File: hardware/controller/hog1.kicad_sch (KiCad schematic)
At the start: 59 parts, among them J4 Conn_01x01, J5 Conn_01x01, J6 Conn_01x01, J7 Conn_01x03, J8 Conn_01x03, Q2 YJD60N04A, Q3 YJD60N04A, Q4 YJD60N04A, Q5 YJD60N04A, Q6 YJD60N04A, Q7 YJD60N04A, U10 LMV331, U11 LM2105D, U12 LMV331, U13 LM2105D, U14 LMV331, U9 LM2105D

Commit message: footprints, layout
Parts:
- removed J7, J8: Conn_01x03, symbol Connector_Generic:Conn_01x03
- removed Q2, Q3, Q4, Q5, Q6, Q7: YJD60N04A, symbol Simulation_SPICE:NMOS
- added J8: Conn_02x03_Odd_Even, Connector_PinHeader_2.54mm:PinHeader_2x03_P2.54mm_Horizontal, symbol Connector_Generic:Conn_02x03_Odd_Even
- added Q2, Q3, Q4, Q5, Q6, Q7: AOD66406, Package_TO_SOT_SMD:TO-252-2, symbol Device:Q_NMOS_DGS
- C36: renamed from C34; footprint (none) -> Capacitor_SMD:C_0603_1608Metric
- C37: renamed from C35; footprint (none) -> Capacitor_SMD:C_0603_1608Metric
- C38: renamed from C36; footprint (none) -> Capacitor_SMD:C_0603_1608Metric
- C39: renamed from C37; footprint (none) -> Capacitor_SMD:CP_Elec_6.3x7.7
- C40: renamed from C38; footprint (none) -> Capacitor_SMD:C_0603_1608Metric
- C41: renamed from C39; footprint (none) -> Capacitor_SMD:C_0603_1608Metric
- C42: renamed from C40; footprint (none) -> Capacitor_SMD:C_0603_1608Metric
- C43: renamed from C41; footprint (none) -> Capacitor_SMD:C_0603_1608Metric
- C44: renamed from C42; footprint (none) -> Capacitor_SMD:CP_Elec_6.3x7.7
- C45: renamed from C43; footprint (none) -> Capacitor_SMD:C_0603_1608Metric
- C46: renamed from C44; footprint (none) -> Capacitor_SMD:C_0603_1608Metric
- C47: renamed from C45; footprint (none) -> Capacitor_SMD:C_0603_1608Metric
- C48: renamed from C46; footprint (none) -> Capacitor_SMD:C_0603_1608Metric
- C49: renamed from C47; footprint (none) -> Capacitor_SMD:CP_Elec_6.3x7.7
- C50: renamed from C48; footprint (none) -> Capacitor_SMD:C_0603_1608Metric
- C51: renamed from C49; footprint (none) -> Capacitor_SMD:C_0603_1608Metric
- C52: renamed from C50; footprint (none) -> Capacitor_SMD:C_0603_1608Metric
- C53: renamed from C51; footprint (none) -> Capacitor_SMD:C_0603_1608Metric
- C54: footprint (none) -> Capacitor_SMD:C_0603_1608Metric
- C55: renamed from C53; footprint (none) -> Capacitor_SMD:C_0603_1608Metric
- C56: renamed from C52; footprint (none) -> Capacitor_SMD:C_0603_1608Metric
- J5: renamed from J4; footprint (none) -> Connector_Wire:SolderWire-2.5sqmm_1x01_D2.4mm_OD4.4mm
- J6: renamed from J5; footprint (none) -> Connector_Wire:SolderWire-2.5sqmm_1x01_D2.4mm_OD4.4mm
- J7: renamed from J6; footprint (none) -> Connector_Wire:SolderWire-2.5sqmm_1x01_D2.4mm_OD4.4mm
- JP1, JP2, JP3: footprint (none) -> Jumper:SolderJumper-3_P1.3mm_Open_RoundedPad1.0x1.5mm
- R19, R20, R21, R22, R23, R24, R25, R26, R27, R28, R29, R30, R31, R32, R33, R34, R35, R36: footprint (none) -> Resistor_SMD:R_0603_1608Metric
- U11: renamed from U12; footprint (none) -> Package_TO_SOT_SMD:SOT-23-5
- U13: renamed from U14; footprint (none) -> Package_TO_SOT_SMD:SOT-23-5
- U9: renamed from U10; footprint (none) -> Package_TO_SOT_SMD:SOT-23-5
- renumbered U11 to U10, U13 to U12, U9 to U8
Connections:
- net +5V: now also J8.3 (Pin_3), J8.4 (Pin_4)
- net GND: now also J8.5 (Pin_5), J8.6 (Pin_6), Q3.3 (S), Q5.3 (S), Q7.3 (S)
- net PHASE_U: now also Q2.3 (S), Q3.1 (D)
- net PHASE_V: now also Q4.3 (S), Q5.1 (D)
- net PHASE_W: now also Q6.3 (S), Q7.1 (D)
- net SERVO1_PWM_X: now also J8.1 (Pin_1)
- net SERVO1_PWM_Y: now also J8.2 (Pin_2)
- net VBUS: now also Q2.1 (D), Q4.1 (D), Q6.1 (D)
- net at R30.2: now also Q5.2 (G)
- net at R25.2: now also Q4.2 (G)
- net at R32.2: now also Q6.2 (G)
- net at R23.2: now also Q3.2 (G)
- net at R19.2: now also Q2.2 (G)
- net at R36.2: now also Q7.2 (G)
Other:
- moved on the sheet: C54, C55, C56

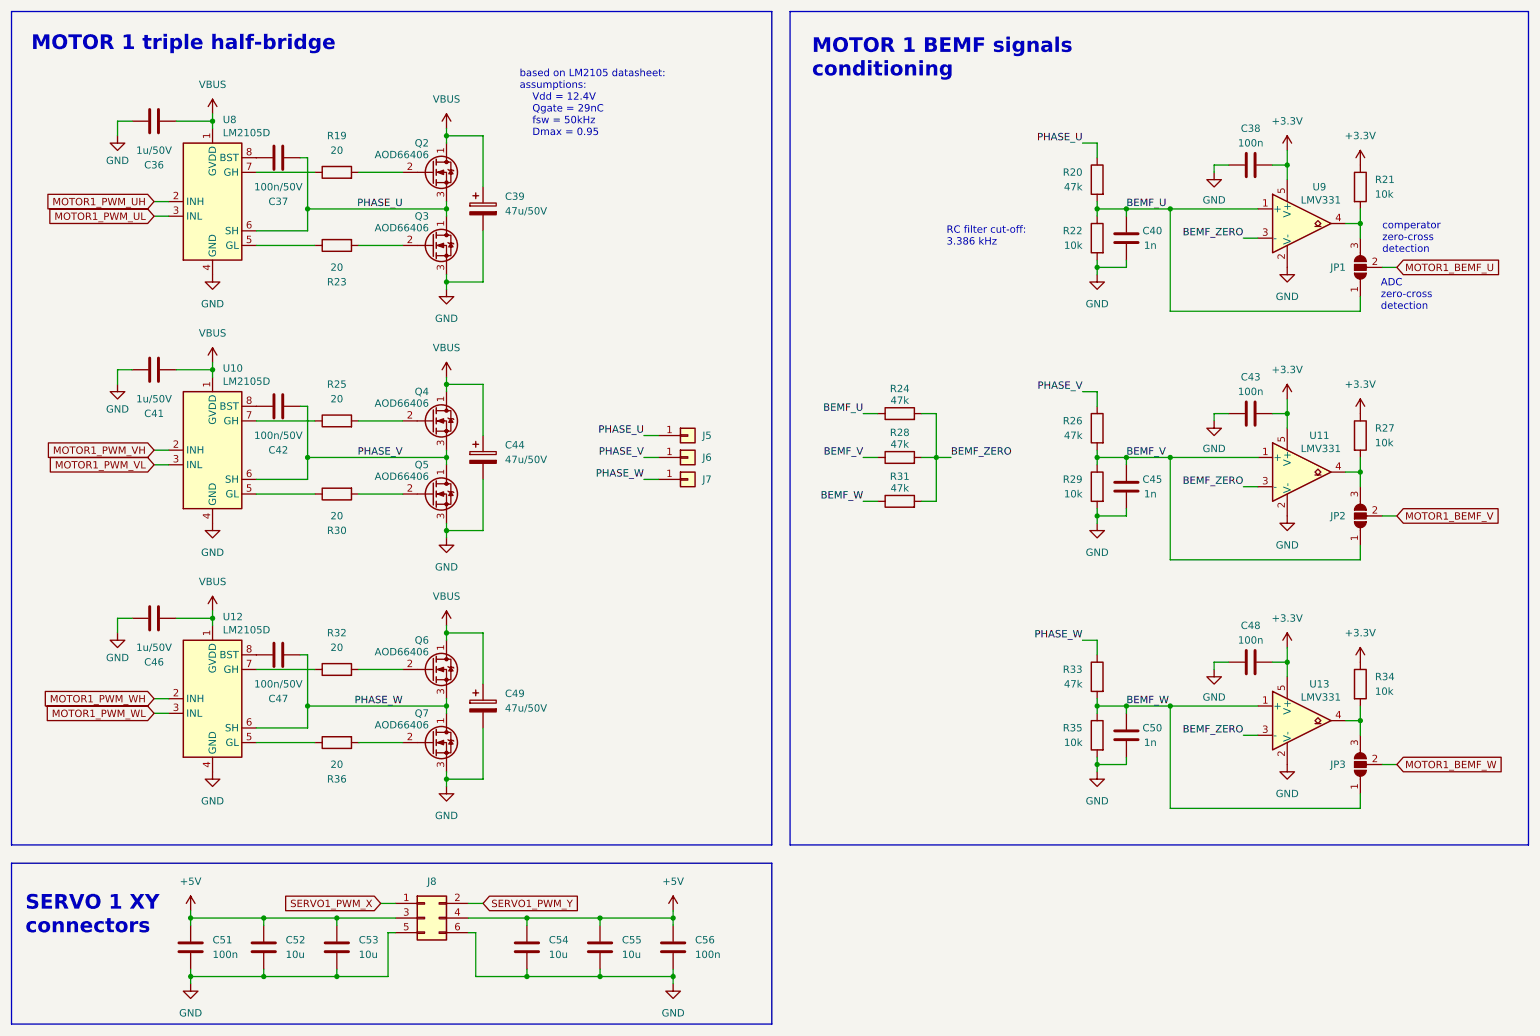
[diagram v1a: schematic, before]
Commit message: add VBUS sense to STM and ESP, change buttons and sw to vertical, add USB-C to SEM
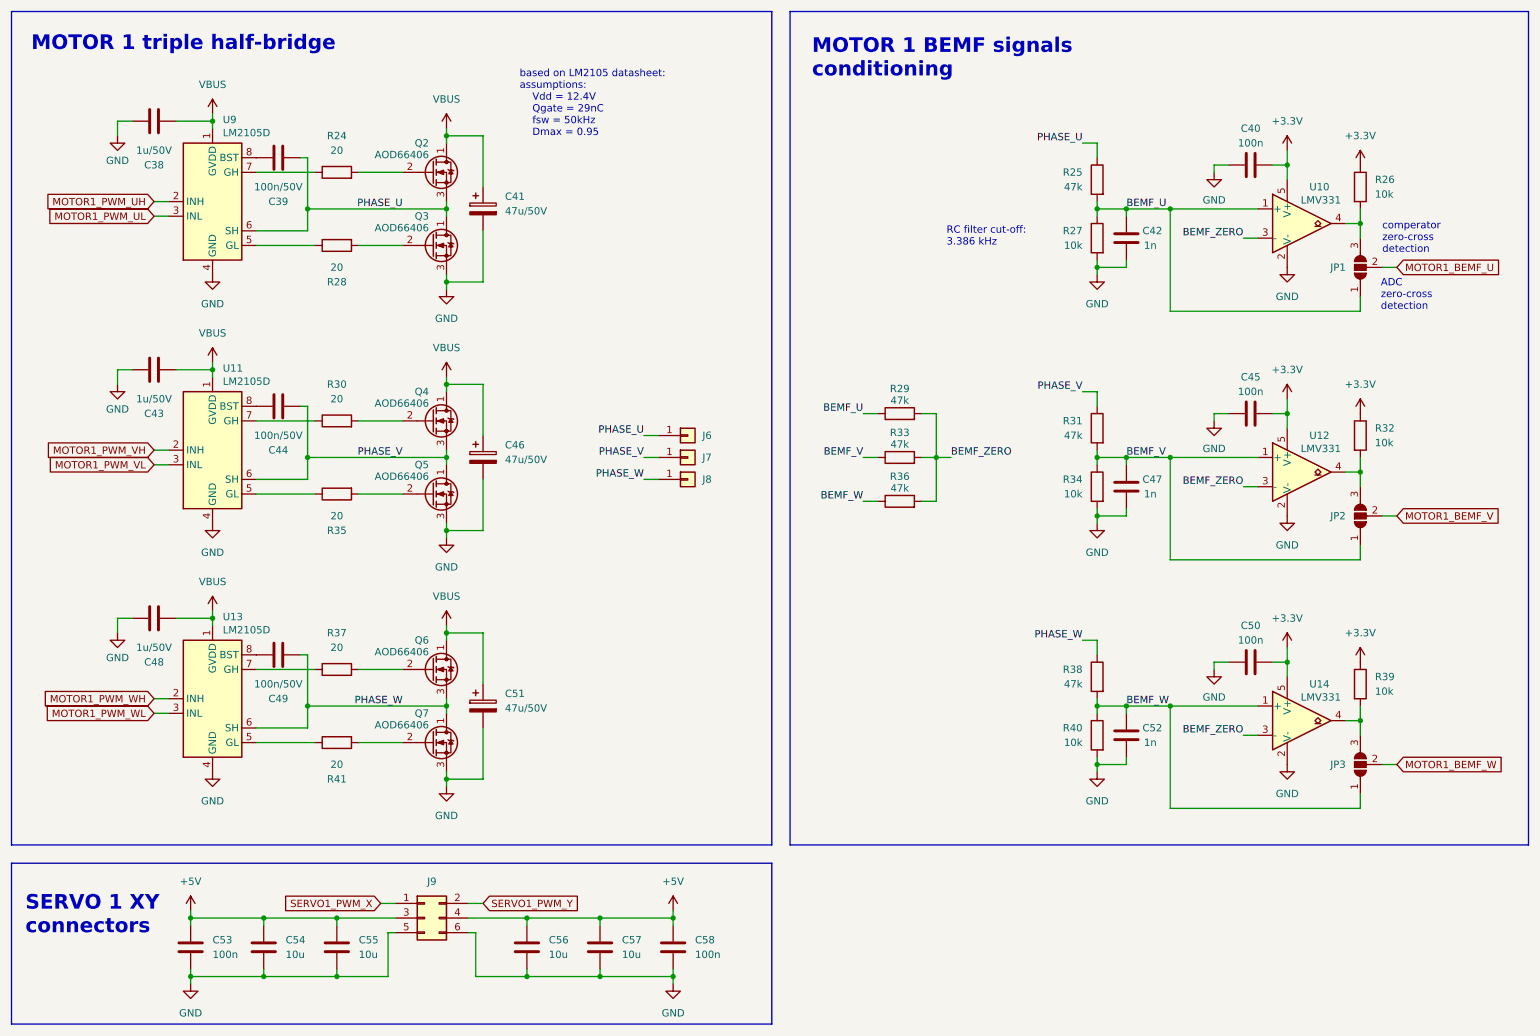
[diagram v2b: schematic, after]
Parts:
- renumbered C36 to C38, C37 to C39, C38 to C40, C39 to C41, C40 to C42, C41 to C43, C42 to C44, C43 to C45, C44 to C46, C45 to C47, C46 to C48, C47 to C49, C48 to C50, C49 to C51, C50 to C52, C51 to C53, C52 to C54, C53 to C55, C54 to C56, C55 to C57, C56 to C58, J5 to J6, J6 to J7, J7 to J8, J8 to J9, R19 to R24, R20 to R25, R21 to R26, R22 to R27, R23 to R28, R24 to R29, R25 to R30, R26 to R31, R27 to R32, R28 to R33, R29 to R34, R30 to R35, R31 to R36, R32 to R37, R33 to R38, R34 to R39, R35 to R40, R36 to R41, U9 to U10, U10 to U11, U11 to U12, U12 to U13, U13 to U14, U8 to U9

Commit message: USBLC6, IR2101
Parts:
- removed U11, U13, U9: LM2105D, Package_SO:SOIC-8_3.9x4.9mm_P1.27mm, symbol Driver_FET:LM2105D
- added D6, D7, D8: 1N5819HW-7-F, Diode_SMD:Nexperia_CFP3_SOD-123W, symbol Device:D_Schottky
- added U11, U13, U9: IR2101, Package_SO:SOIC-8_3.9x4.9mm_P1.27mm, symbol Driver_FET:IR2101
- C39, C44, C49: value 100n/50V -> 1u/50V
- R24, R28, R30, R35, R37, R41: value 20 -> 100
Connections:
- net GND: now also U11.4 (COM), U13.4 (COM), U9.4 (COM)
- net MOTOR1_PWM_UH: now also U9.2 (HIN)
- net MOTOR1_PWM_UL: now also U9.3 (LIN)
- net MOTOR1_PWM_VH: now also U11.2 (HIN)
- net MOTOR1_PWM_VL: now also U11.3 (LIN)
- net MOTOR1_PWM_WH: now also U13.2 (HIN)
- net MOTOR1_PWM_WL: now also U13.3 (LIN)
- net PHASE_U: now also U9.6 (VS)
- net PHASE_V: now also U11.6 (VS)
- net PHASE_W: now also U13.6 (VS)
- net VBUS: now also D6.2 (A), D7.2 (A), D8.2 (A), U11.1 (VCC), U13.1 (VCC), U9.1 (VCC)
- net at R28.1: now also U9.5 (LO)
- net at R24.1: now also U9.7 (HO)
- net at C39.1: now also D6.1 (K), U9.8 (VB)
- net at R30.1: now also U11.7 (HO)
- net at C49.1: now also D8.1 (K), U13.8 (VB)
- net at R35.1: now also U11.5 (LO)
- net at C44.1: now also D7.1 (K), U11.8 (VB)
- net at R37.1: now also U13.7 (HO)
- net at R41.1: now also U13.5 (LO)
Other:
- note removed: "based on LM2105 datasheet: assumptions: Vdd = 12.4V Qgate = 29nC fsw = 50kHz Dmax = 0.95"
- moved on the sheet: C41, C46, C51, Q2, Q3, Q4, Q5, Q6, Q7, R24, R28

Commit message: custom footprints with all 3D models
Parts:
- renumbered C38 to C36, C39 to C37, C40 to C38, C41 to C39, C42 to C40, C43 to C41, C44 to C42, C45 to C43, C46 to C44, C47 to C45, C48 to C46, C49 to C47, C50 to C48, C51 to C49, C52 to C50, C53 to C51, C54 to C52, C55 to C53, C56 to C54, C57 to C55, C58 to C56

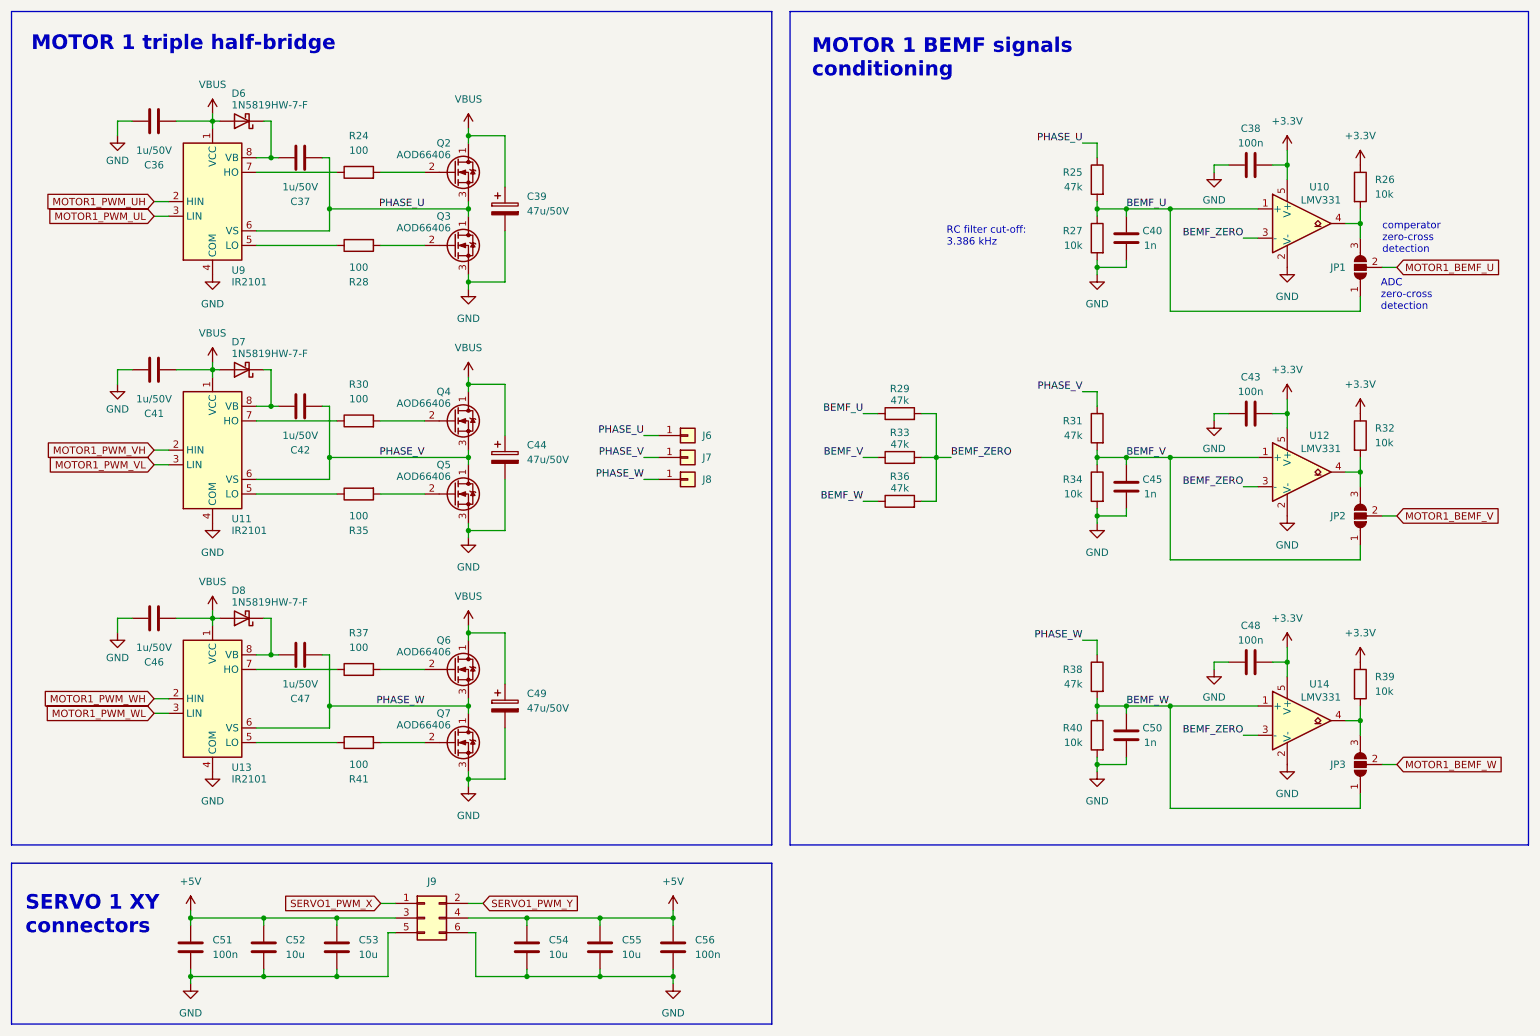
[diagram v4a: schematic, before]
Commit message: back to LM2105, remove USB-C from STM
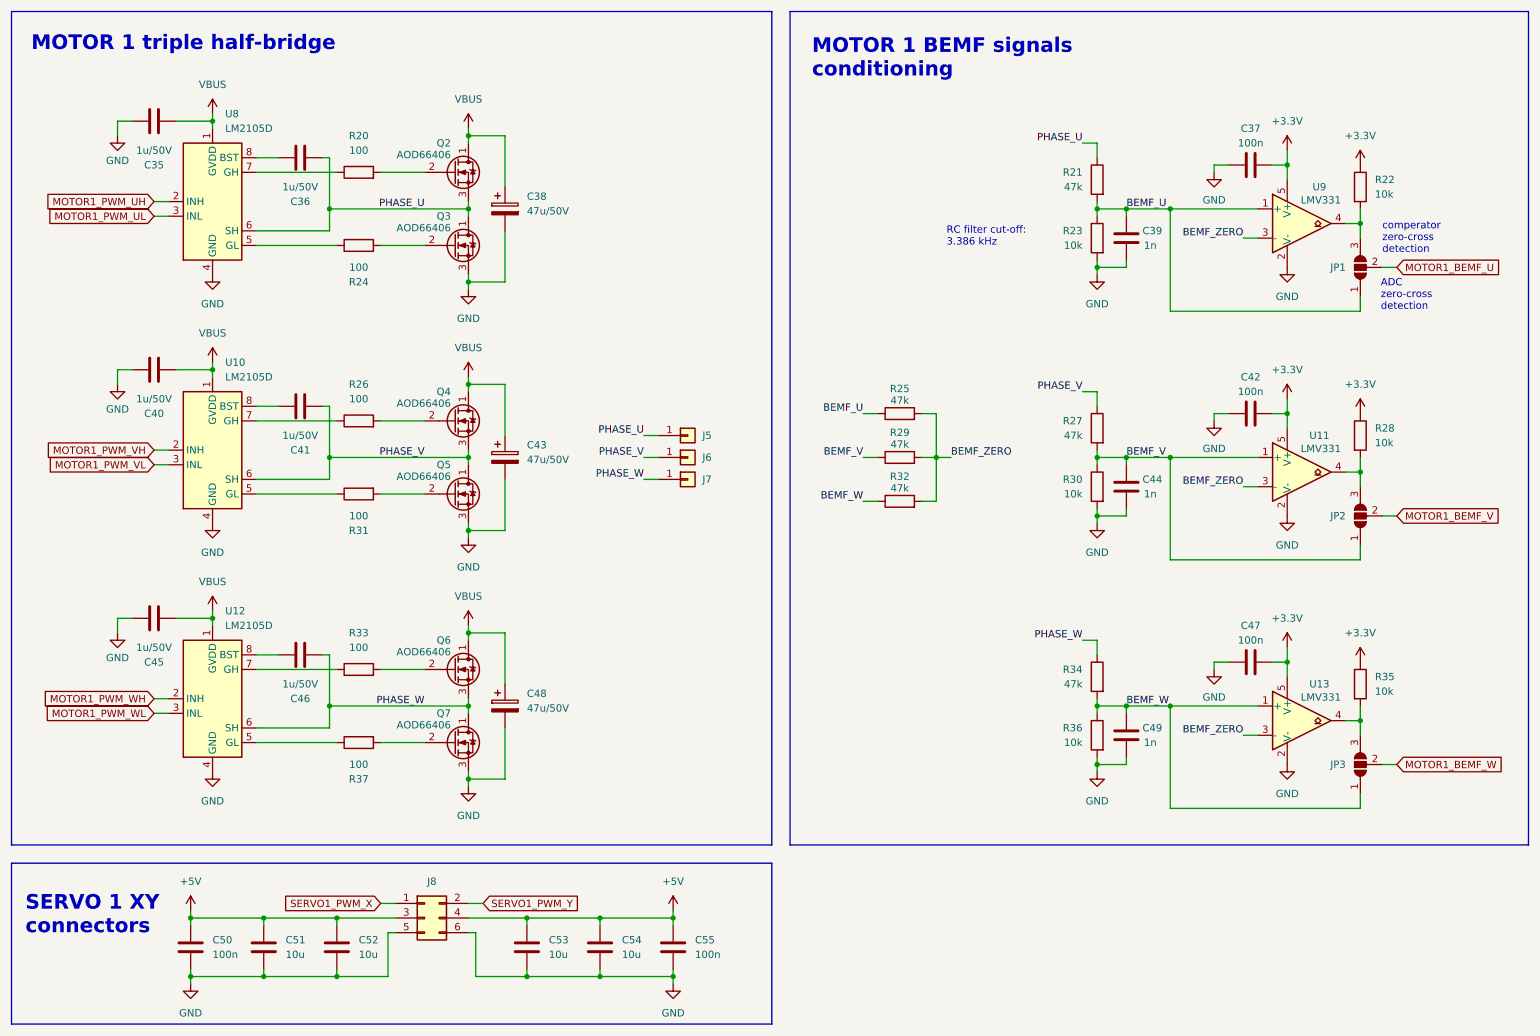
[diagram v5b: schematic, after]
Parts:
- removed D6, D7, D8: 1N5819HW-7-F, Diode_SMD:Nexperia_CFP3_SOD-123W, symbol Device:D_Schottky
- removed U11, U13, U9: IR2101, Package_SO:SOIC-8_3.9x4.9mm_P1.27mm, symbol Driver_FET:IR2101
- added U10, U12, U8: LM2105D, Package_SO:SOIC-8_3.9x4.9mm_P1.27mm, symbol Driver_FET:LM2105D
- renumbered C36 to C35, C37 to C36, C38 to C37, C39 to C38, C40 to C39, C41 to C40, C42 to C41, C43 to C42, C44 to C43, C45 to C44, C46 to C45, C47 to C46, C48 to C47, C49 to C48, C50 to C49, C51 to C50, C52 to C51, C53 to C52, C54 to C53, C55 to C54, C56 to C55, J6 to J5, J7 to J6, J8 to J7, J9 to J8, R24 to R20, R25 to R21, R26 to R22, R27 to R23, R28 to R24, R29 to R25, R30 to R26, R31 to R27, R32 to R28, R33 to R29, R34 to R30, R35 to R31, R36 to R32, R37 to R33, R38 to R34, R39 to R35, R40 to R36, R41 to R37, U12 to U11, U14 to U13, U10 to U9
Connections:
- net GND: now also U10.4 (GND), U12.4 (GND), U8.4 (GND)
- net MOTOR1_PWM_UH: now also U8.2 (INH)
- net MOTOR1_PWM_UL: now also U8.3 (INL)
- net MOTOR1_PWM_VH: now also U10.2 (INH)
- net MOTOR1_PWM_VL: now also U10.3 (INL)
- net MOTOR1_PWM_WH: now also U12.2 (INH)
- net MOTOR1_PWM_WL: now also U12.3 (INL)
- net PHASE_U: now also U8.6 (SH)
- net PHASE_V: now also U10.6 (SH)
- net PHASE_W: now also U12.6 (SH)
- net VBUS: now also U10.1 (GVDD), U12.1 (GVDD), U8.1 (GVDD)
- net at C41.1: now also U10.8 (BST)
- net at C46.1: now also U12.8 (BST)
- net at R33.1: now also U12.7 (GH)
- net at R24.1: now also U8.5 (GL)
- net at R20.1: now also U8.7 (GH)
- net at C36.1: now also U8.8 (BST)
- net at R31.1: now also U10.5 (GL)
- net at R26.1: now also U10.7 (GH)
- net at R37.1: now also U12.5 (GL)
